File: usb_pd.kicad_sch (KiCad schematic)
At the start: 1 part

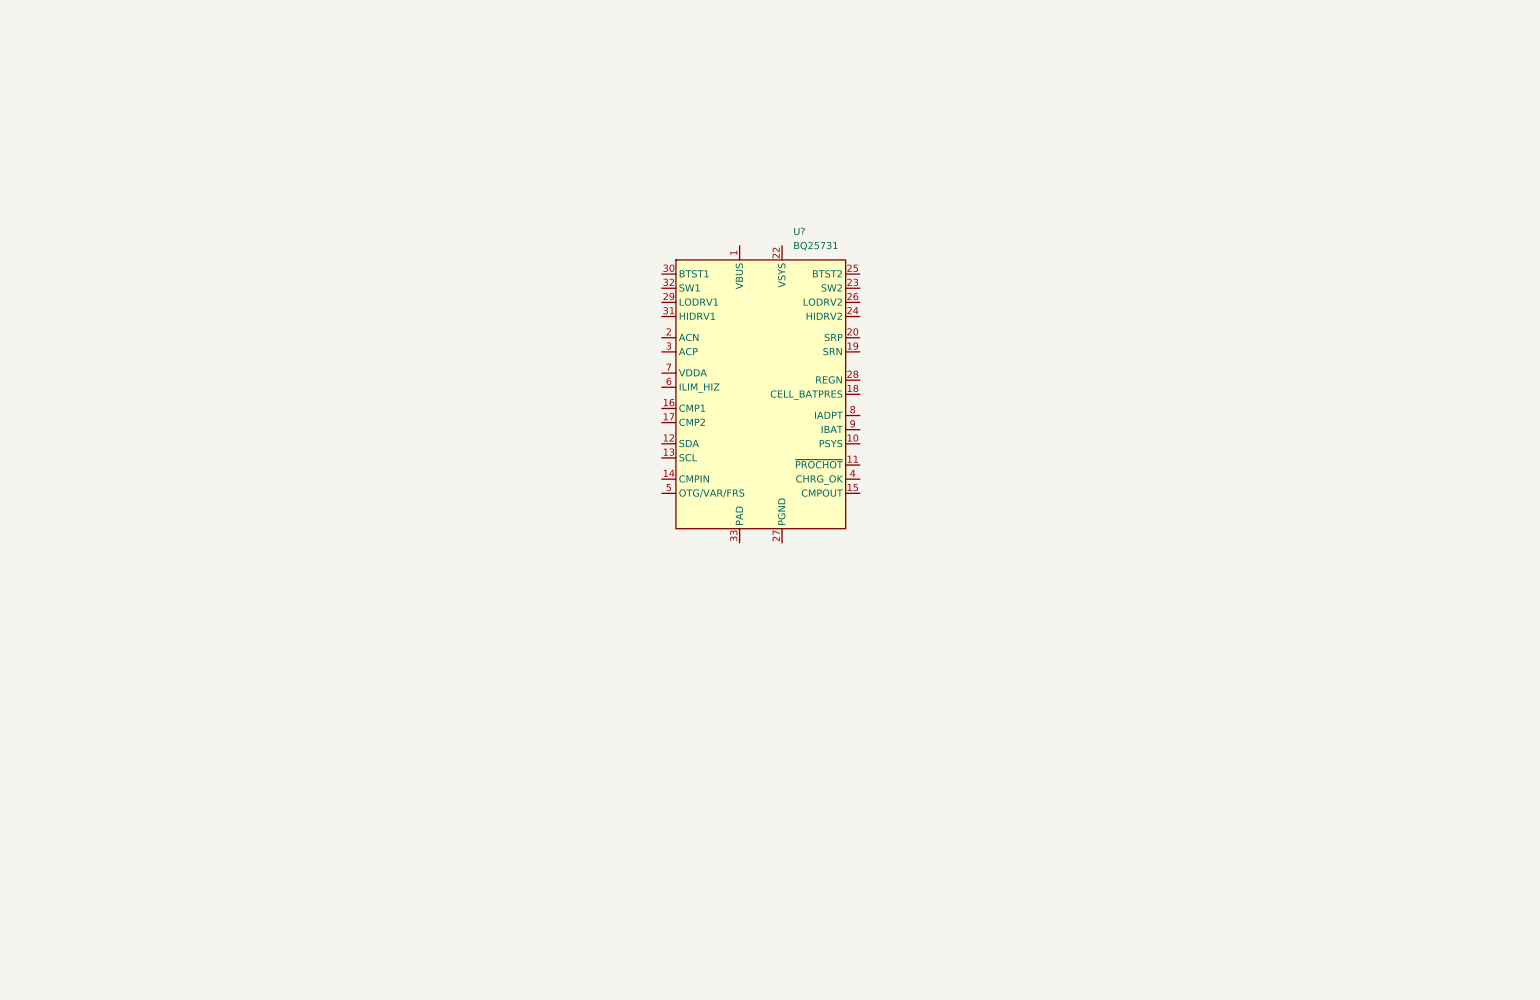
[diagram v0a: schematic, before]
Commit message: added lora, gps, nfc schematics
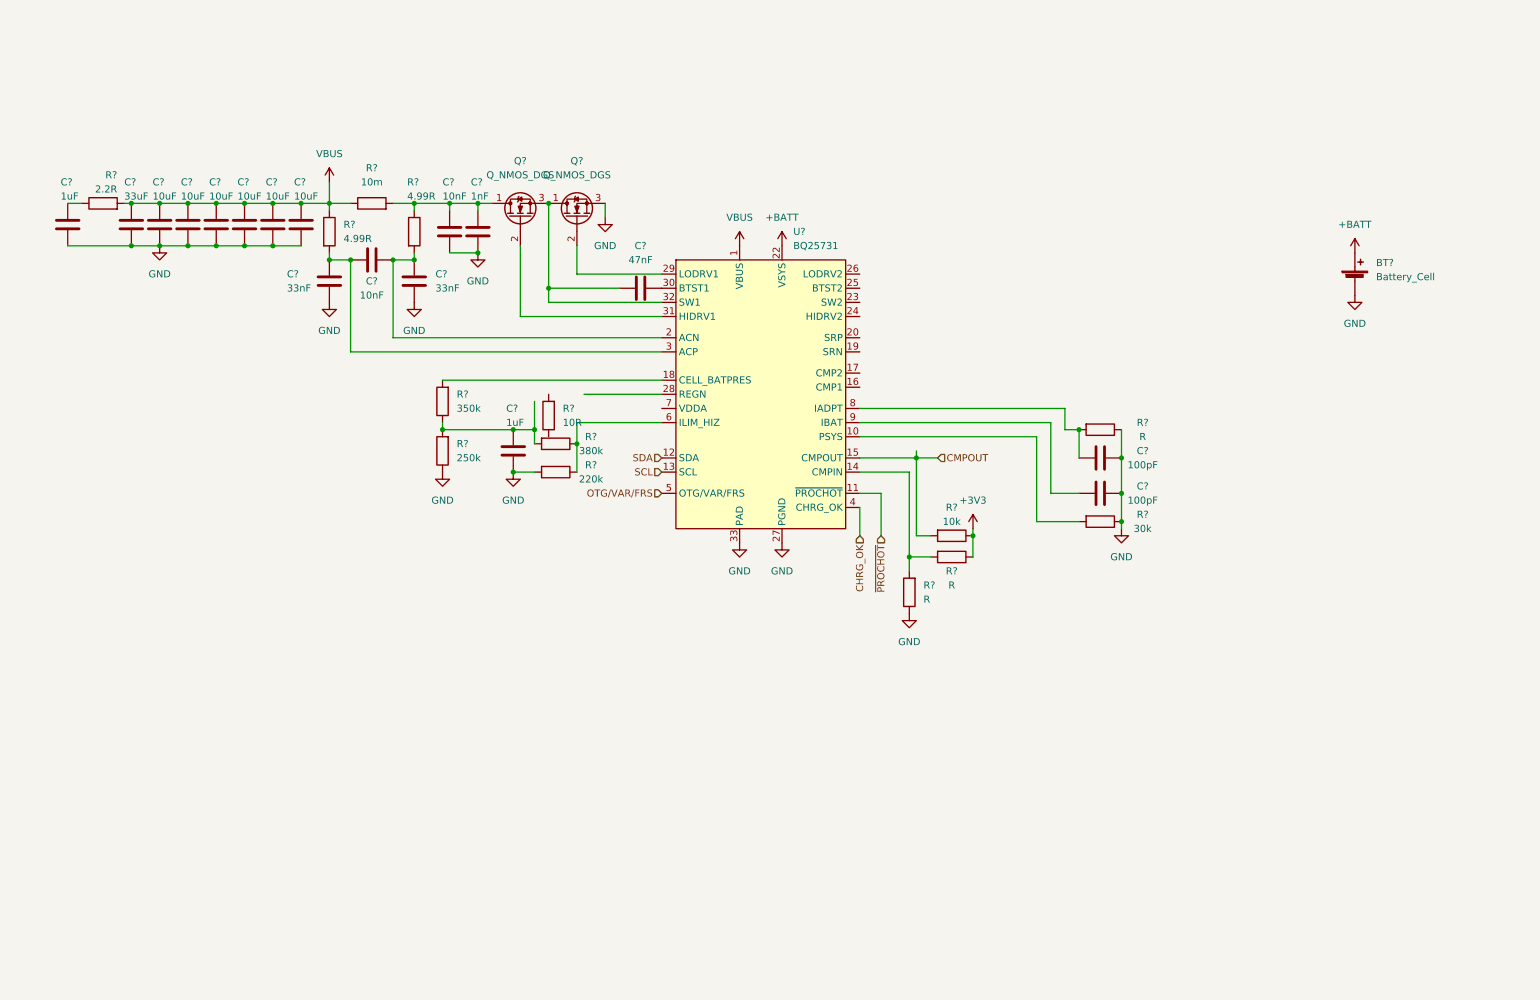
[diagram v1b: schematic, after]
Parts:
- added BT?: Battery_Cell, symbol Device:Battery_Cell
- added C?: 1nF, symbol Device:C
- added C?: 47nF, symbol Device:C
- added C? (x2): 33nF, symbol Device:C
- added C? (x2): 10nF, symbol Device:C
- added C? (x2): 1uF, symbol Device:C
- added C? (x6): 10uF, symbol Device:C
- added C? (x2): 100pF, symbol Device:C
- added C?: 33uF, symbol Device:C
- added Q? (x2): Q_NMOS_DGS, symbol Device:Q_NMOS_DGS
- added R? (x2): 4.99R, symbol Device:R
- added R?: 220k, symbol Device:R
- added R? (x3): R, symbol Device:R
- added R?: 10m, symbol Device:R
- added R?: 2.2R, symbol Device:R
- added R?: 10R, symbol Device:R
- added R?: 350k, symbol Device:R
- added R?: 30k, symbol Device:R
- added R?: 250k, symbol Device:R
- added R?: 380k, symbol Device:R
- added R?: 10k, symbol Device:R
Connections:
- net VBUS: now reaches U?.1 (VBUS)
- net VBUS: now also C?.2, C?.2, C?.2, C?.2, C?.2, C?.2, C?.2, R?.1, R?.1, R?.2
- net at U?.10 (PSYS): now also R?.2
- net ~{PROCHOT}: now reaches U?.11 (~{PROCHOT})
- net SDA: now reaches U?.12 (SDA)
- net SCL: now reaches U?.13 (SCL)
- net at U?.14 (CMPIN): now also R?.2, R?.2
- net CMPOUT: now reaches U?.15 (CMPOUT)
- net CMPOUT: now also R?.2
- net at U?.18 (CELL_BATPRES): now also R?.2
- net at U?.2 (ACN): now also C?.1, C?.2, R?.2
- net +BATT: now reaches U?.22 (VSYS)
- net +BATT: now also BT?.1 (+)
- net GND: now reaches U?.27 (PGND)
- net GND: now also U?.33 (PAD), BT?.2 (-), C?.1, C?.1, C?.1, C?.1, C?.1, C?.1, C?.1, C?.1, C?.1, C?.1, C?.1, C?.1, C?.1, C?.2, C?.2, Q?.3 (S), R?.1, R?.1, R?.1, R?.1, R?.2
- net at U?.29 (LODRV1): now also Q?.2 (G)
- net at U?.3 (ACP): now also C?.1, C?.2, R?.2
- net at U?.30 (BTST1): now also C?.1
- net at U?.31 (HIDRV1): now also Q?.2 (G)
- net at U?.32 (SW1): now also C?.2, Q?.1 (D), Q?.3 (S)
- net CHRG_OK: now reaches U?.4 (CHRG_OK)
- net OTG/VAR/FRS: now reaches U?.5 (OTG/VAR/FRS)
- net at U?.6 (ILIM_HIZ): now also R?.1, R?.1
- net at U?.8 (IADPT): now also C?.1, R?.2
- net at U?.9 (IBAT): now also C?.2
- new net: C?.2, C?.2, Q?.1 (D), R?.1, R?.2
- new net: C?.2, R?.1
- new net: C?.2, R?.1, R?.2, R?.2
- new net +3V3: R?.1, R?.1

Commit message: Added display, update lora sym, updated usb-pd schematic, connected sd, added external buttons
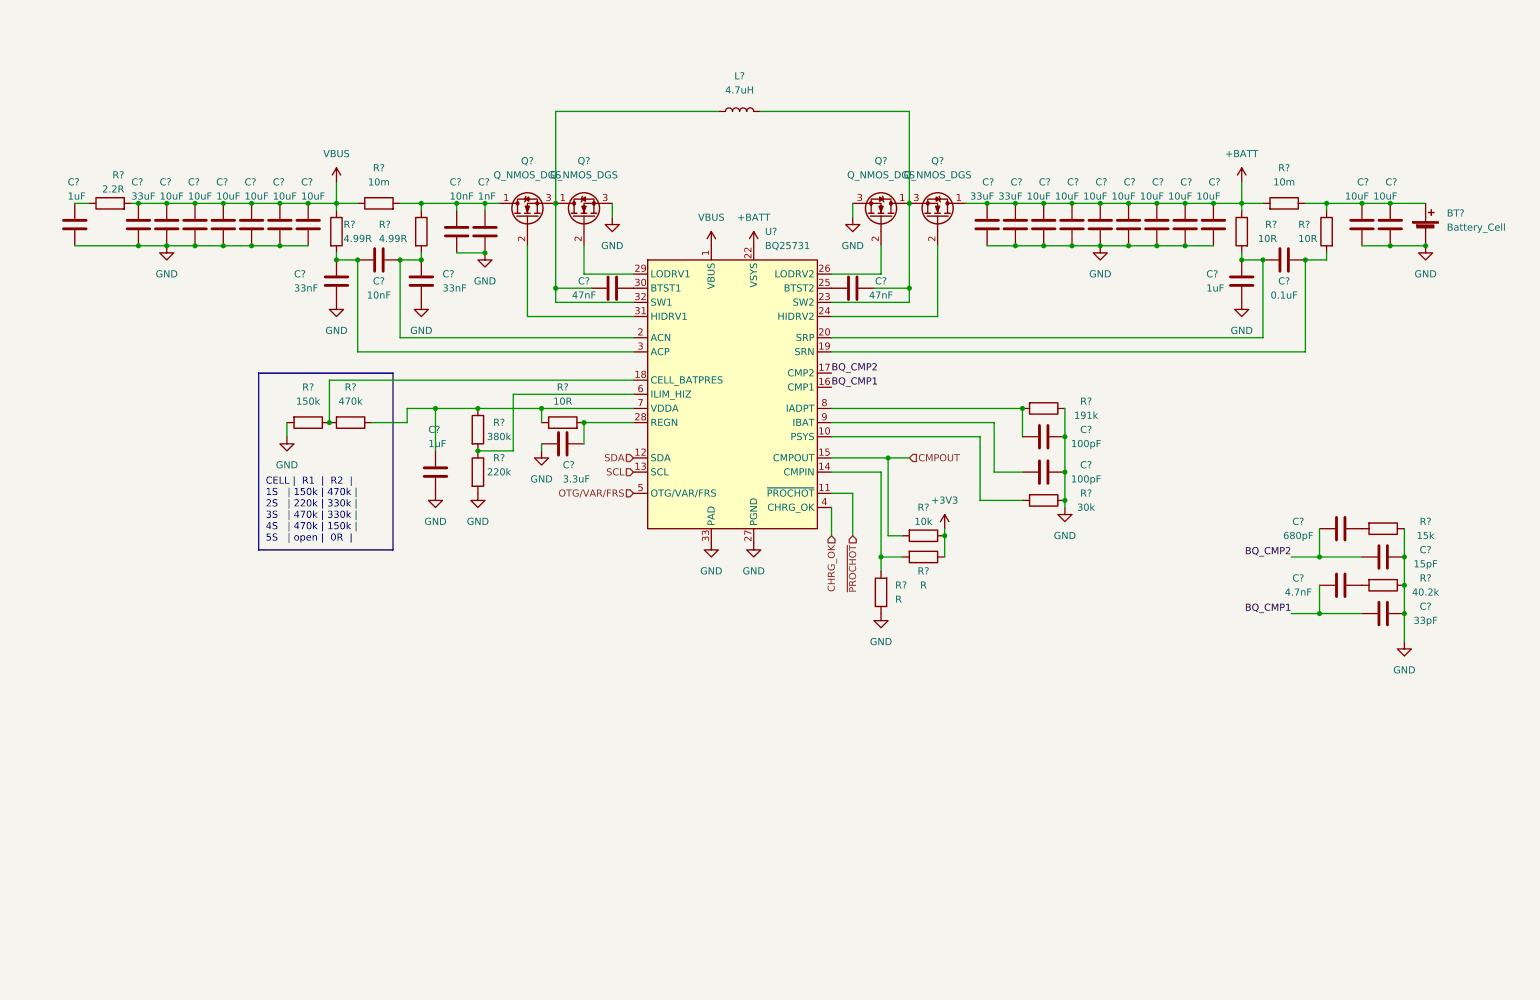
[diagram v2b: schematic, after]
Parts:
- added C? (x9): 10uF, symbol Device:C
- added C?: 4.7nF, symbol Device:C
- added C?: 0.1uF, symbol Device:C
- added C?: 680pF, symbol Device:C
- added C? (x2): 33uF, symbol Device:C
- added C?: 33pF, symbol Device:C
- added C?: 3.3uF, symbol Device:C
- added C?: 1uF, symbol Device:C
- added C?: 15pF, symbol Device:C
- added C?: 47nF, symbol Device:C
- added L?: 4.7uH, symbol Device:L
- added Q? (x2): Q_NMOS_DGS, symbol Device:Q_NMOS_DGS
- added R? (x2): 10R, symbol Device:R
- added R?: 10m, symbol Device:R
- added R?: 40.2k, symbol Device:R
- added R?: 15k, symbol Device:R
- R?: value 350k -> 470k
- R?: value 250k -> 150k
- R?: value R -> 191k
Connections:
- net +BATT: now also C?.2, C?.2, C?.2, C?.2, C?.2, C?.2, C?.2, C?.2, C?.2, Q?.1 (D), R?.1, R?.2; no longer BT?.1 (+)
- net GND: now also R?.2, C?.1, C?.1, C?.1, C?.1, C?.1, C?.1, C?.1, C?.1, C?.1, C?.1, C?.1, C?.1, C?.2, C?.2, C?.2, Q?.3 (S), R?.1, R?.1; no longer R?.1
- net at R?.1, U?.6 (ILIM_HIZ): now also R?.2; no longer R?.1
- net at C?.2, Q?.1 (D), Q?.3 (S)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: now also L?.1
- net at C?.2, R?.1: now also R?.1, R?.1, U?.7 (VDDA); no longer R?.2, R?.2
- net at R?.2: now also U?.28 (REGN), C?.2
- net at R?.2, U?.18 (CELL_BATPRES): now also R?.1
- net BQ_CMP1: now reaches U?.16 (CMP1)
- net BQ_CMP1: now also C?.1, C?.1
- net BQ_CMP2: now reaches U?.17 (CMP2)
- net BQ_CMP2: now also C?.1, C?.1
- net at U?.19 (SRN): now also C?.1, R?.2
- net at U?.20 (SRP): now also C?.1, C?.2, R?.2
- net at U?.23 (SW2): now also C?.2, L?.2, Q?.1 (D), Q?.3 (S)
- net at U?.24 (HIDRV2): now also Q?.2 (G)
- net at U?.25 (BTST2): now also C?.1
- net at U?.26 (LODRV2): now also Q?.2 (G)
- new net: BT?.1 (+), C?.2, C?.2, R?.1, R?.1
- new net: C?.2, R?.2 (x2)
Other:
- note added: "CELL | R1 | R2 | 1S | 150k | 470k | 2S | 220k | 330k | 3S | 470k | 330k | 4S | 470k | 150k | 5S | open | 0R |"
- moved on the sheet: BT?, C?, Q?, R?, U?

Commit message: Added new lora, added rgb leds, updated TSP65988 schematic, added bat to 3v3, added battery balancer
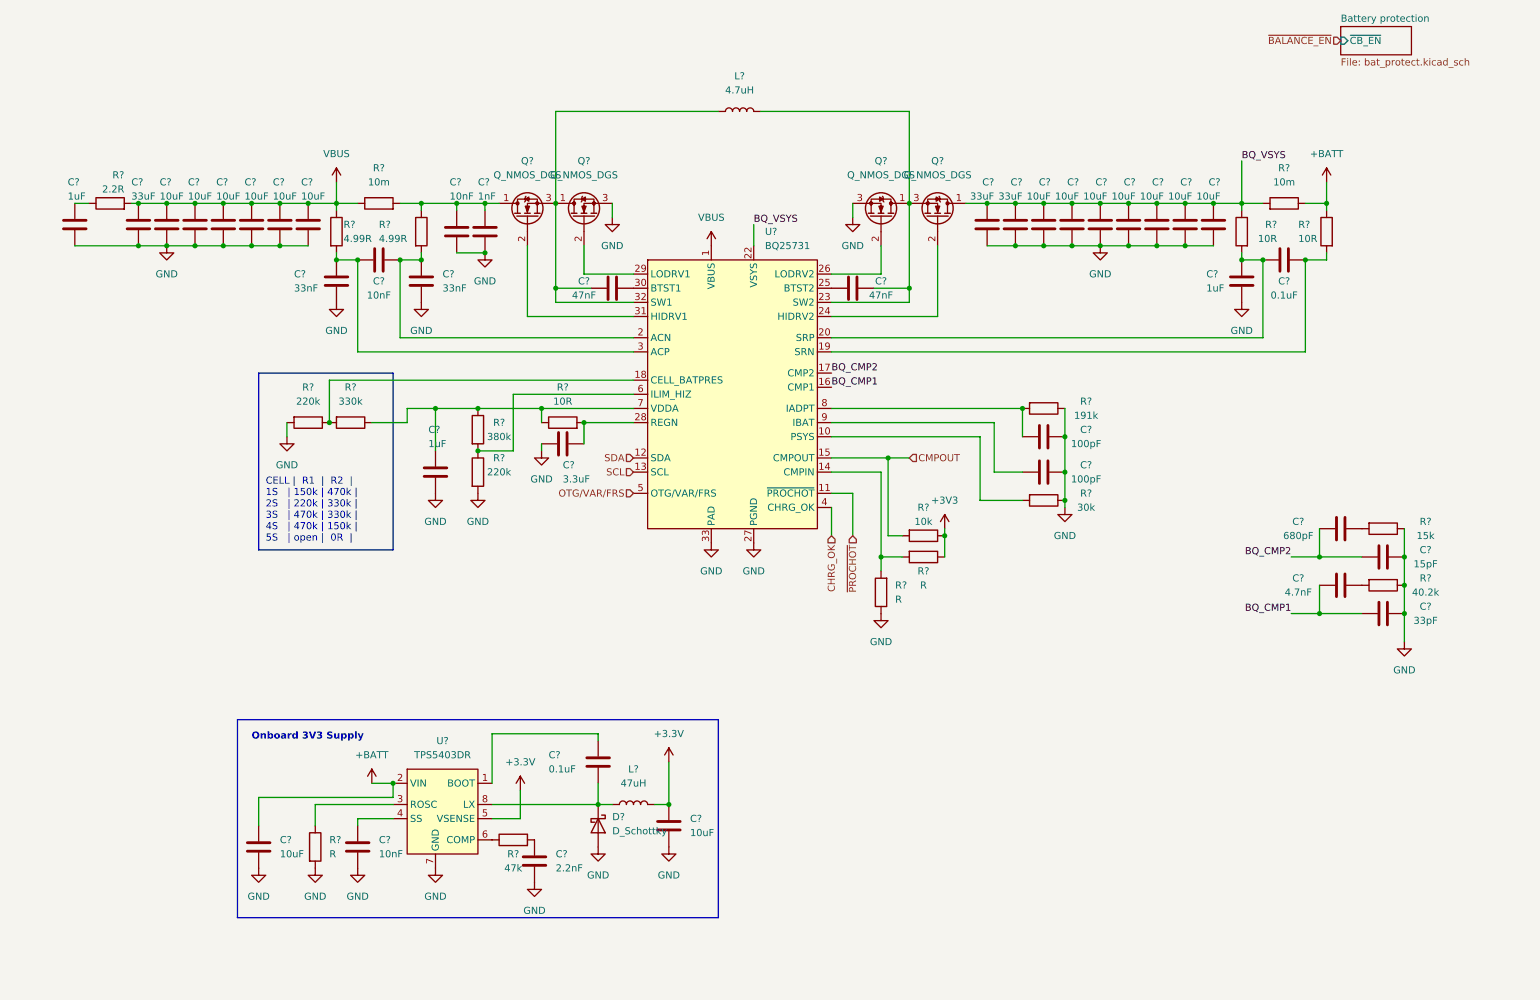
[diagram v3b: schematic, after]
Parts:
- removed BT?: Battery_Cell, symbol Device:Battery_Cell
- removed C? (x2): 10uF, symbol Device:C
- added C? (x2): 10uF, Capacitor_SMD:C_0805_2012Metric_Pad1.18x1.45mm_HandSolder, symbol Device:C
- added C?: 10nF, Capacitor_SMD:C_0603_1608Metric_Pad1.08x0.95mm_HandSolder, symbol Device:C
- added C?: 0.1uF, Capacitor_SMD:C_0603_1608Metric_Pad1.08x0.95mm_HandSolder, symbol Device:C
- added C?: 2.2nF, Capacitor_SMD:C_0603_1608Metric_Pad1.08x0.95mm_HandSolder, symbol Device:C
- added D?: D_Schottky, Diode_SMD:D_SMB, symbol Device:D_Schottky
- added L?: 47uH, smarthome:Inductor_104CDMCC, symbol Device:L
- added R?: 47k, Resistor_SMD:R_0603_1608Metric_Pad0.98x0.95mm_HandSolder, symbol Device:R
- added R?: R, Resistor_SMD:R_0603_1608Metric_Pad0.98x0.95mm_HandSolder, symbol Device:R
- added U?: TPS5403DR, Package_SO:SOIC-8_3.9x4.9mm_P1.27mm, symbol smarthome:TPS5403DR
- R?: value 470k -> 330k
- R?: value 150k -> 220k
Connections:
- net +3V3: now also C?.2, L?.2, U?.5 (VSENSE)
- net +BATT: now also R?.1, R?.1, C?.2, U?.2 (VIN); no longer C?.2, C?.2, C?.2, C?.2, C?.2, C?.2, C?.2, C?.2, C?.2, Q?.1 (D), R?.1, R?.2, U?.22 (VSYS)
- net GND: now also C?.1, C?.1, C?.2, C?.2, D?.2 (A), R?.2, U?.7 (GND)
- new net: C?.1, U?.4 (SS)
- new net: C?.2, D?.1 (K), L?.1, U?.8 (LX)
- new net: R?.1, U?.6 (COMP)
- new net: C?.1, R?.2
- new net: R?.1, U?.3 (ROSC)
- new net: C?.1, U?.1 (BOOT)
- new net BQ_VSYS: C?.2, C?.2, C?.2, C?.2, C?.2, C?.2, C?.2, C?.2, C?.2, Q?.1 (D), R?.1, R?.2, U?.22 (VSYS)
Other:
- added sheet Battery protection (bat_protect.kicad_sch)
- note added: "Onboard 3V3 Supply"
